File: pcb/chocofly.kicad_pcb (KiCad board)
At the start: 2 copper layers, 317 x 133.4 mm, 142 parts, among them P1 battery+, P2 battery-, SW1 SW_Push, SW11 SW_Push, SW12 SW_Push, SW13 SW_Push, SW14 SW_Push, SW15 SW_Push, SW16 SW_Push, SW17 SW_Push, SW18 SW_Push, SW19 SW_Push, SW2 SW_Push, SW20 SW_Push, SW21 SW_Push, SW22 SW_Push, SW23 SW_Push, SW24 SW_Push, SW25 SW_Push, SW26 SW_Push, SW27 SW_Push, SW28 SW_Push, SW29 SW_Push, SW3 SW_Push, SW30 SW_Push, SW31 SW_Push, SW32 SW_Push, SW33 SW_Push, SW34 SW_Push, SW35 SW_Push, SW36 SW_Push, SW37 SW_Push, SW38 SW_Push, SW39 SW_Push, SW4 SW_Push, SW40 SW_Push, SW41 SW_Push, SW42 SW_Push, SW43 SW_Push, SW44 SW_Push, SW45 SW_Push, SW46 SW_Push, SW47 SW_Push, SW48 SW_Push, SW49 SW_Push, SW5 SW_Push, SW50 SW_Push, SW51 SW_Push, SW52 SW_Push, SW53 SW_Push, SW54 SW_Push, SW55 SW_Push, SW56 SW_Push, SW57 SW_Push, SW58 SW_Push, SW59 SW_Push, SW6 SW_Push, SW60 SW_Push, SW61 SW_Push, SW62 Reset, SW63 Power, SW7 SW_Push, SW8 SW_Push, SW9 SW_Push

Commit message: Edge cuts are so cool.
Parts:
- moved SW63 16.4 mm to (23.8, -18.8)
- moved SW62 16.3 mm to (-22.2, -18.3)
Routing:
- net row0: track 121.0 -> 92.9 mm, vias 5 -> 3
- net row1: track 136.8 -> 109.1 mm, vias 6 -> 4
- net Net-(MCU1-Pad24): track 41.1 -> 24.0 mm
- net Net-(P1-Pad1): track 22.6 -> 6.10 mm, vias 1 -> 0
- net GND: track 83.8 -> 70.5 mm
- net Net-(MCU1-Pad22): track 26.4 -> 14.9 mm
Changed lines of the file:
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@@
   (general
     (thickness 1.6)
-    (drawings 78)
-    (tracks 204)
+    (drawings 79)
+    (tracks 174)
     (zones 0)
     (modules 142)
@@
     (0 F.Cu signal)
     (31 B.Cu signal)
-    (32 B.Adhes user hide)
-    (33 F.Adhes user hide)
-    (34 B.Paste user hide)
-    (35 F.Paste user hide)
-    (36 B.SilkS user hide)
-    (37 F.SilkS user hide)
-    (38 B.Mask user hide)
-    (39 F.Mask user hide)
+    (32 B.Adhes user)
+    (33 F.Adhes user)
+    (34 B.Paste user)
+    (35 F.Paste user)
+    (36 B.SilkS user)
+    (37 F.SilkS user)
+    (38 B.Mask user)
+    (39 F.Mask user)
     (40 Dwgs.User user)
     (41 Cmts.User user)
@@
   )
   (module footprints:Switch_Reset_THT (layer F.Cu)
-    (at -17.979997 -34.039998 346.5)
+    (at -22.229997 -18.289998 346.5)
     (fp_text reference SW62 (at 0.000001 0.01 166.5) (layer Dwgs.User) hide
       (effects (font (size 1 1) (thickness 0.15)))
@@
   )
   (module footprints:Switch_MSK-12C01-07 (layer F.Cu)
-    (at 21.87 -35.11 193.5)
+    (at 23.82 -18.81 193.5)
     (fp_text reference SW63 (at -4.937662 -2.502587 193.5) (layer F.SilkS)
       (effects (font (size 1 1) (thickness 0.15)))
@@
     (pad 1 np_thru_hole circle (at 0 0) (size 2.2 2.2) (drill 2.2) (layers *.Cu *.Mask))
   )
+  (dimension 116.65 (width 0.15) (layer Dwgs.User)
+    (gr_text "116,650 mm" (at 173.7 17.775 90) (layer Dwgs.User)
+      (effects (font (size 1 1) (thickness 0.15)))
+    )
+    (feature1 (pts (xy 152.9 -40.55) (xy 172.986421 -40.55)))
+    (feature2 (pts (xy 152.9 76.1) (xy 172.986421 76.1)))
+    (crossbar (pts (xy 172.4 76.1) (xy 172.4 -40.55)))
+    (arrow1a (pts (xy 172.4 -40.55) (xy 172.986421 -39.423496)))
+    (arrow1b (pts (xy 172.4 -40.55) (xy 171.813579 -39.423496)))
+    (arrow2a (pts (xy 172.4 76.1) (xy 172.986421 74.973496)))
+    (arrow2b (pts (xy 172.4 76.1) (xy 171.813579 74.973496)))
+  )
   (gr_line (start 158.500001 -52.299987) (end 158.500001 -38.85) (layer Edge.Cuts) (width 0.05))
   (gr_arc (start 153.5 -35.53) (end 153.500013 -41.530001) (angle 56.41572066) (layer Edge.Cuts) (width 0.05))
@@
   (gr_line (start -158.5 -35.529996) (end -158.5 5.674075) (layer Edge.Cuts) (width 0.05))
   (gr_text "Chocofly v2.0 by vitvlkv\nhttps://github.com/vlkv/chocofly" (at -96.5 28.9 -13.5) (layer B.SilkS)
-    (effects (font (size 2 2) (thickness 0.3)) (justify left mirror))
+    (effects (font (size 1.8 1.8) (thickness 0.3)) (justify left mirror))
   )
   (gr_text "Chocofly v2.0 by vitvlkv\nhttps://github.com/vlkv/chocofly" (at 98.8 28.5 13.5) (layer F.SilkS)
-    (effects (font (size 2 2) (thickness 0.3)) (justify left))
+    (effects (font (size 1.8 1.8) (thickness 0.3)) (justify left))
   )
-  (gr_text "Power\n" (at 29.05 -37 13.5) (layer F.SilkS)
+  (gr_text "Power\n" (at 31 -20.7 13.5) (layer F.SilkS)
     (effects (font (size 1 1) (thickness 0.15)))
   )
-  (gr_text "Reset\n" (at -24.58 -36.74 -13.5) (layer F.SilkS)
+  (gr_text "Reset\n" (at -28.83 -20.99 -13.5) (layer F.SilkS)
     (effects (font (size 1 1) (thickness 0.15)))
   )
@@
   (via (at 10.200002 -3.821907) (size 0.5) (drill 0.3) (layers F.Cu B.Cu) (net 1))
   (segment (start 7.608095 -3.821905) (end 10.200002 -3.821907) (width 0.25) (layer F.Cu) (net 1) (status 10))
-  (segment (start -17.6 -27.2) (end -17.680619 -27.28062) (width 0.25) (layer B.Cu) (net 1))
-  (segment (start -11.600002 -21.200001) (end -17.6 -27.2) (width 0.25) (layer B.Cu) (net 1))
   (segment (start -11.6 11.4) (end -11.600002 -21.200001) (width 0.25) (layer B.Cu) (net 1))
   (segment (start -8 15.8) (end 10.199999 15.8) (width 0.25) (layer F.Cu) (net 1))
   (segment (start -11.6 12.2) (end -8 15.8) (width 0.25) (layer F.Cu) (net 1))
   (segment (start -11.6 11.4) (end -11.6 12.2) (width 0.25) (layer F.Cu) (net 1))
-  (segment (start -19.8 -29.4) (end -17.6 -27.2) (width 0.25) (layer B.Cu) (net 1))
-  (via (at -18.357145 -29.4) (size 0.5) (drill 0.3) (layers F.Cu B.Cu) (net 1))
-  (via (at 21.797616 -29.397616) (size 0.5) (drill 0.3) (layers F.Cu B.Cu) (net 1))
-  (segment (start 10.199999 -17.799999) (end 21.797616 -29.397616) (width 0.25) (layer B.Cu) (net 1))
   (segment (start 10.199999 -3.8) (end 10.199999 -17.799999) (width 0.25) (layer B.Cu) (net 1))
   (via (at -5.2 -3.8) (size 0.5) (drill 0.3) (layers F.Cu B.Cu) (net 3))
@@
   (segment (start 11 16.599999) (end 11 -1.281905) (width 0.25) (layer B.Cu) (net 16))
   (segment (start 7.608095 -1.281905) (end 11.000004 -1.280008) (width 0.25) (layer F.Cu) (net 16) (status 10))
-  (segment (start 11.000004 -17.338756) (end 15.130624 -21.469375) (width 0.25) (layer B.Cu) (net 16))
-  (segment (start 14.720017 -21.058766) (end 15.130624 -21.469375) (width 0.25) (layer B.Cu) (net 16))
   (segment (start 11.000002 -15.799997) (end 11.000004 -17.338756) (width 0.25) (layer B.Cu) (net 16))
   (segment (start 11.000004 -1.280008) (end 11.000002 -15.799997) (width 0.25) (layer B.Cu) (net 16))
-  (segment (start -18.600002 -26.999998) (end -18.769373 -27.16937) (width 0.25) (layer B.Cu) (net 16))
-  (segment (start -12.400001 -20.799999) (end -18.600002 -26.999998) (width 0.25) (layer B.Cu) (net 16))
   (segment (start -12.4 11.4) (end -12.400001 -20.799999) (width 0.25) (layer B.Cu) (net 16))
   (segment (start 11 16.599999) (end -8.2 16.599999) (width 0.25) (layer F.Cu) (net 16))
@@
   (segment (start -12.4 12.4) (end -8.2 16.599999) (width 0.25) (layer F.Cu) (net 16))
   (segment (start -12.4 11.4) (end -12.4 12.4) (width 0.25) (layer F.Cu) (net 16))
-  (segment (start -20.2 -28.599999) (end -18.600002 -26.999998) (width 0.25) (layer B.Cu) (net 16))
-  (via (at -18.757145 -28.599999) (size 0.5) (drill 0.3) (layers F.Cu B.Cu) (net 16))
-  (segment (start 15.130624 -21.469375) (end 22.2 -28.6) (width 0.25) (layer B.Cu) (net 16))
-  (via (at 22.2 -28.6) (size 0.5) (drill 0.3) (layers F.Cu B.Cu) (net 16))
   (via (at -13.2 11.399999) (size 0.5) (drill 0.3) (layers F.Cu B.Cu) (net 29))
   (via (at 11.799999 17.397562) (size 0.5) (drill 0.3) (layers F.Cu B.Cu) (net 29))
@@
   (segment (start -7.631905 -13.981905) (end 0.581905 -13.981905) (width 0.5) (layer F.Cu) (net 80) (status 10))
   (segment (start 4.181905 -13.981905) (end 6.6 -16.4) (width 0.5) (layer F.Cu) (net 80))
-  (segment (start 18.4 -22.8) (end 12 -16.4) (width 0.5) (layer F.Cu) (net 80))
   (segment (start 6.6 -16.4) (end 12 -16.4) (width 0.5) (layer F.Cu) (net 80))
-  (segment (start 18.4 -30.8) (end 18.4 -22.8) (width 0.5) (layer F.Cu) (net 80))
   (segment (start -7.574381 -8.844388) (end -7.619991 -8.890005) (width 0.5) (layer F.Cu) (net 81) (status 30))
   (segment (start -10 -11.27) (end -7.631904 -8.901906) (width 0.25) (layer B.Cu) (net 81) (status 20))
@@
   (segment (start -10 -12.2) (end -10 -11.27) (width 0.25) (layer B.Cu) (net 81))
   (segment (start -10 -22) (end -10 -12.2) (width 0.25) (layer B.Cu) (net 81))
-  (segment (start -17.97999 -29.979992) (end -12.4 -24.400001) (width 0.25) (layer B.Cu) (net 81))
-  (segment (start -12.4 -24.400001) (end -10 -22) (width 0.25) (layer B.Cu) (net 81))
-  (segment (start -12.530625 -24.530629) (end -12.4 -24.400001) (width 0.25) (layer B.Cu) (net 81))
   (segment (start 7.608091 -6.361908) (end 7.608095 -8.901905) (width 0.5) (layer B.Cu) (net 82) (status 30))
   (via (at -10.799999 -11.440022) (size 0.5) (drill 0.3) (layers F.Cu B.Cu) (net 82))
@@
   (segment (start -7.631905 -11.441905) (end -10.799999 -11.440022) (width 0.25) (layer F.Cu) (net 82) (status 10))
   (segment (start -10.8 -21.6) (end -10.799995 14.4) (width 0.25) (layer B.Cu) (net 82))
-  (segment (start -16.000002 -26.799999) (end -10.8 -21.6) (width 0.25) (layer B.Cu) (net 82))
-  (segment (start -18.779986 -29.579984) (end -16.000002 -26.799999) (width 0.25) (layer B.Cu) (net 82))
-  (segment (start -16.369376 -27.169373) (end -16.000002 -26.799999) (width 0.25) (layer B.Cu) (net 82))
-  (segment (start -21.140199 -34.798696) (end -20.538696 -34.798697) (width 0.25) (layer B.Cu) (net 82) (status 30))
-  (segment (start -21.140199 -34.798696) (end -20.738696 -34.798696) (width 0.25) (layer B.Cu) (net 82) (status 30))
-  (segment (start -21.140199 -34.798696) (end -20.718682 -34.798696) (width 0.25) (layer B.Cu) (net 82) (status 30))
   (segment (start 0.540001 -8.901905) (end -2 -11.441906) (width 0.5) (layer F.Cu) (net 82))
   (segment (start 7.608095 -8.901905) (end 0.540001 -8.901905) (width 0.5) (layer F.Cu) (net 82) (status 10))
@@
   (segment (start 4 -16.6) (end 7.30125 -16.6) (width 0.5) (layer B.Cu) (net 83) (status 10))
   (segment (start 7.620014 -16.918764) (end 8.450625 -17.749375) (width 0.5) (layer B.Cu) (net 83))
-  (segment (start 16.634229 -30.834229) (end 16.634229 -26.034229) (width 0.5) (layer F.Cu) (net 83))
-  (via (at 16.634229 -26.034229) (size 0.6) (drill 0.4) (layers F.Cu B.Cu) (net 83))
-  (segment (start 16.634229 -25.965771) (end 16.650625 -25.949375) (width 0.5) (layer B.Cu) (net 83))
-  (segment (start 16.634229 -26.034229) (end 16.634229 -25.965771) (width 0.5) (layer B.Cu) (net 83))
-  (segment (start 8.450625 -17.749375) (end 16.650625 -25.949375) (width 0.5) (layer B.Cu) (net 83))
 )

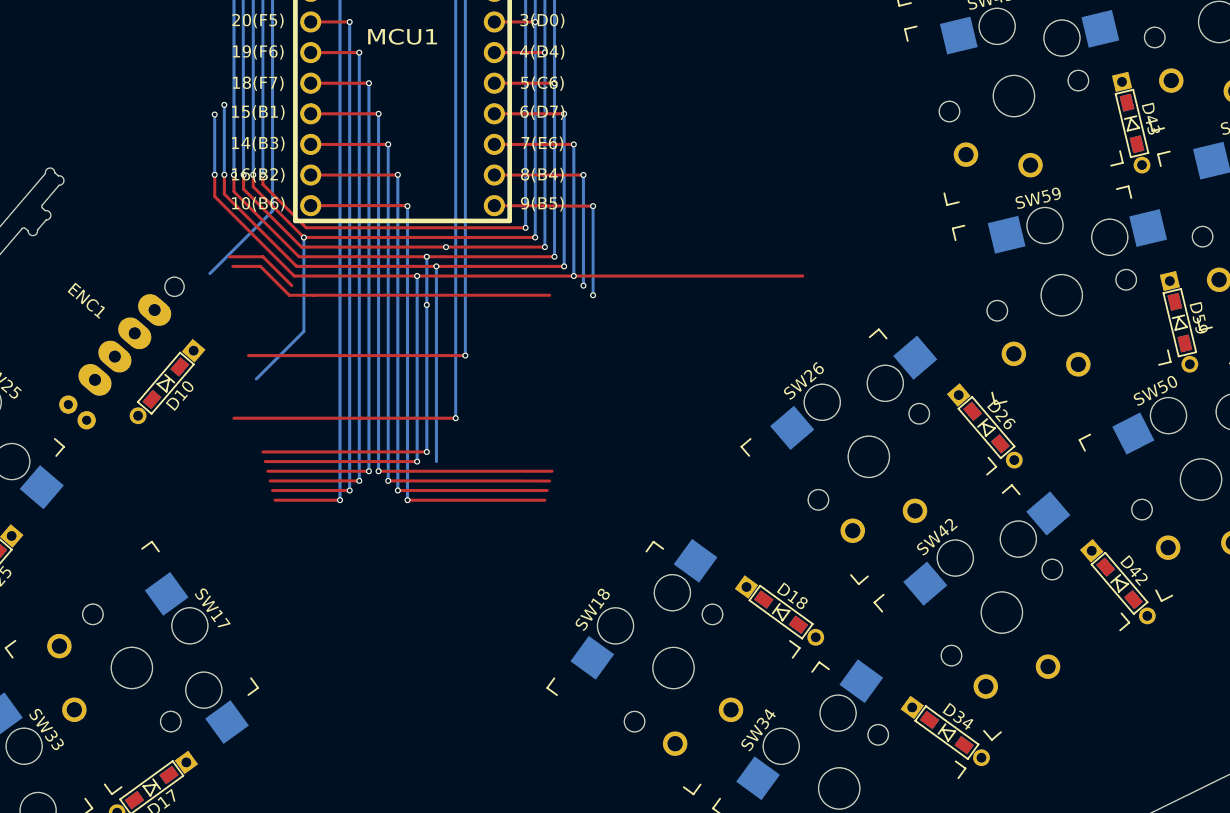
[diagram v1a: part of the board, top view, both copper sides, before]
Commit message: Added one more encoder
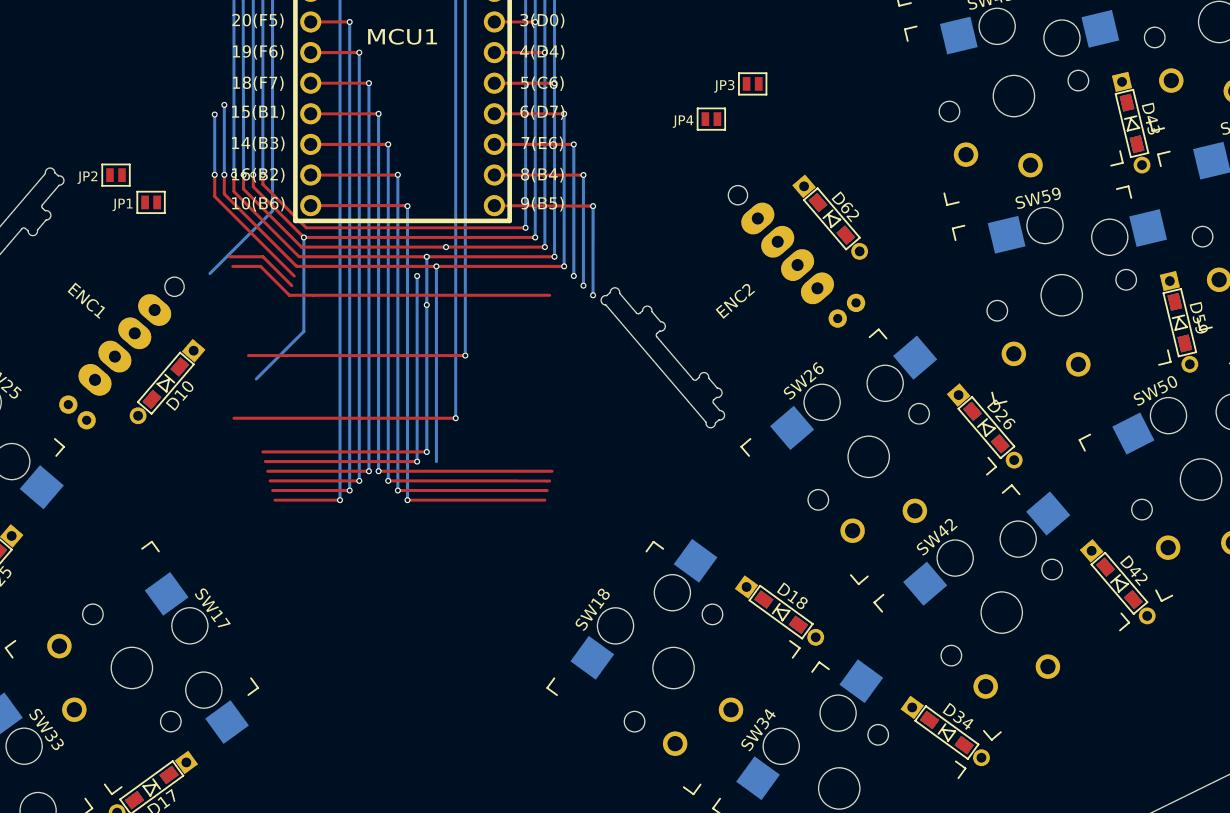
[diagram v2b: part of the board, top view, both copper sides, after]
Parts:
- added D62: 1N4148, footprints:diode_TH_SMD, F.Cu at (35.6, 15.1)
- added ENC2: EVQWGD001, footprints:EVQWGD001, F.Cu at (27.6, 21.9)
- added JP1: Jumper_NC_Small, footprints:avalanche_Jumper, F.Cu at (-20.9, 13.7)
- added JP2: Jumper_NC_Small, footprints:avalanche_Jumper, F.Cu at (-23.8, 11.4)
- added JP3: Jumper_NC_Small, footprints:avalanche_Jumper, F.Cu at (29.0, 3.86)
- added JP4: Jumper_NC_Small, footprints:avalanche_Jumper, F.Cu at (25.6, 6.78)
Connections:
- ENC1 pad A: encA -> Net-(ENC1-PadA)
- ENC1 pad B: encB -> Net-(ENC1-PadB)
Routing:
- net row5: track 103.8 -> 61.6 mm

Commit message: Ready to wire
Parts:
- moved H15 252.4 mm to (-70.1, 150.4), turned to 0 degrees
- moved H11 240.7 mm to (-76.1, 150.4), turned to 0 degrees
- moved H22 216.8 mm to (-58.2, 150.4)
- moved H4 209.9 mm to (-82.0, 150.4)
- moved H2 185.6 mm to (-82.0, 144.4)
- moved H10 152.2 mm to (-70.1, 138.5)
- moved H18 151.4 mm to (-58.2, 138.5)
- moved H1 125.5 mm to (-82.0, 138.5)
- moved H13 97.7 mm to (-64.2, 138.5)
- moved H16 91.3 mm to (-64.2, 144.4), turned to 0 degrees
- moved H3 90.2 mm to (-76.1, 138.5), turned to 0 degrees
- moved H21 87.6 mm to (-58.2, 144.4)
- moved H6 74.7 mm to (-76.1, 144.4)
- moved H12 63.0 mm to (-70.1, 144.4)
- moved H20 22.6 mm to (-64.2, 150.4)
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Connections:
- JP1 pad 1: encA -> Net-(ENC1-PadA)
- JP1 pad 2: Net-(ENC1-PadA) -> encA
- JP2 pad 1: encB -> Net-(ENC1-PadB)
- JP2 pad 2: Net-(ENC1-PadB) -> encB
- JP3 pad 1: encA -> Net-(ENC2-PadA)
- JP3 pad 2: Net-(ENC2-PadA) -> encA
- JP4 pad 1: encB -> Net-(ENC2-PadB)
- JP4 pad 2: Net-(ENC2-PadB) -> encB
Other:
- outline, holes or cut-outs redrawn
- board text added: "Angle 4 degrees Angle 13,5 degrees"

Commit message: Wiring...
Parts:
- moved H18 60.8 mm to (-87.7, 85.3), turned to 13.5 degrees
- moved H21 60.3 mm to (-86.3, 91.1), turned to 13.5 degrees
- moved H22 59.8 mm to (-85.0, 96.9), turned to 13.5 degrees
- moved H13 59.5 mm to (-93.5, 86.7), turned to 13.5 degrees
- moved H16 59.0 mm to (-92.1, 92.5), turned to 13.5 degrees
- moved H20 58.5 mm to (-90.7, 98.3), turned to 13.5 degrees
- moved H10 58.2 mm to (-99.3, 88.1), turned to 13.5 degrees
- moved H12 57.7 mm to (-97.9, 93.9), turned to 13.5 degrees
- moved H15 57.2 mm to (-96.5, 99.7), turned to 13.5 degrees
- moved H3 56.9 mm to (-105.1, 89.5), turned to 13.5 degrees
- moved H6 56.4 mm to (-103.7, 95.3), turned to 13.5 degrees
- moved H11 55.9 mm to (-102.3, 101.1), turned to 13.5 degrees
- moved H1 55.7 mm to (-110.9, 90.9), turned to 13.5 degrees
- moved H2 55.1 mm to (-109.5, 96.7), turned to 13.5 degrees
- moved H4 54.6 mm to (-108.1, 102.4), turned to 13.5 degrees
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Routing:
- net col2: track 46.9 -> 297.4 mm
- net col0: track 50.1 -> 293.8 mm
- net col1: track 48.7 -> 289.5 mm
- net row0: track 92.9 -> 222.4 mm
- net row2: track 85.2 -> 205.4 mm
- net row6: track 22.8 -> 142.2 mm
- net row4: track 72.7 -> 191.9 mm
- net row1: track 109.1 -> 216.6 mm
- net row5: track 61.6 -> 156.7 mm
- net row3: track 117.0 -> 210.2 mm
- net row7: track 42.7 -> 135.9 mm
- net Net-(D46-Pad2): track 0.00 -> 26.6 mm
- net Net-(D7-Pad2): track 0.00 -> 26.6 mm
- net Net-(D1-Pad2): track 0.00 -> 26.6 mm
- net Net-(D16-Pad2): track 0.00 -> 26.6 mm
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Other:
- board size 317 x 133.4 mm -> 322.4 x 174.6 mm

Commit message: WIP
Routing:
- net col3: track 45.4 -> 81.8 mm
- net row7: track 135.9 -> 165.5 mm
- net Net-(D57-Pad2): track 0.00 -> 26.6 mm
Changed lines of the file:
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@@
     (thickness 1.6)
     (drawings 83)
-    (tracks 775)
+    (tracks 802)
     (zones 0)
     (modules 148)
@@
     (38 B.Mask user)
     (39 F.Mask user)
-    (40 Dwgs.User user hide)
-    (41 Cmts.User user hide)
-    (42 Eco1.User user hide)
+    (40 Dwgs.User user)
+    (41 Cmts.User user)
+    (42 Eco1.User user)
     (43 Eco2.User user)
     (44 Edge.Cuts user)
@@
   (segment (start -51.461364 27.622196) (end -51.461364 36.197196) (width 0.25) (layer B.Cu) (net 62))
   (segment (start -39.436364 41.622195) (end -39.436364 39.847195) (width 0.25) (layer B.Cu) (net 62))
+  (segment (start -78.851364 51.427195) (end -75.576364 54.702195) (width 0.25) (layer B.Cu) (net 63))
+  (segment (start -78.851364 42.852195) (end -78.851364 51.427195) (width 0.25) (layer B.Cu) (net 63))
+  (segment (start -66.576363 56.852196) (end -66.576363 55.077196) (width 0.25) (layer F.Cu) (net 63))
+  (segment (start -73.426363 56.852196) (end -75.576364 54.702195) (width 0.25) (layer F.Cu) (net 63))
+  (segment (start -66.576363 56.852196) (end -73.426363 56.852196) (width 0.25) (layer F.Cu) (net 63))
+  (segment (start -66.576363 56.852196) (end -66.576363 55.077196) (width 0.25) (layer B.Cu) (net 63))
   (via (at -4.577683 -0.219325) (size 0.5) (drill 0.3) (layers F.Cu B.Cu) (net 67))
   (segment (start -4.577683 -0.219325) (end 4.499118 37.588269) (width 0.25) (layer B.Cu) (net 67))
@@
   (segment (start -6.534388 5.474786) (end -1.834136 4.346354) (width 0.25) (layer F.Cu) (net 69) (status 10))
   (segment (start -2.486509 37.619904) (end 5.681397 35.658964) (width 0.25) (layer F.Cu) (net 69))
+  (segment (start -65.751364 45.052195) (end -64.2 46.603559) (width 0.25) (layer B.Cu) (net 69))
+  (segment (start -67.301364 45.052195) (end -65.751364 45.052195) (width 0.25) (layer B.Cu) (net 69))
+  (segment (start -64.2 51.058892) (end -61.592315 53.666577) (width 0.25) (layer B.Cu) (net 69))
+  (segment (start -64.2 46.603559) (end -64.2 51.058892) (width 0.25) (layer B.Cu) (net 69))
+  (segment (start -80.576364 52.602195) (end -74.578559 58.6) (width 0.25) (layer F.Cu) (net 69))
+  (segment (start -61.592315 53.666577) (end -61.592315 55.192315) (width 0.25) (layer F.Cu) (net 69))
+  (segment (start -65 58.6) (end -65.2 58.6) (width 0.25) (layer F.Cu) (net 69))
+  (segment (start -61.592315 55.192315) (end -65 58.6) (width 0.25) (layer F.Cu) (net 69))
+  (segment (start -65.2 58.6) (end -65.1 58.6) (width 0.25) (layer F.Cu) (net 69))
+  (segment (start -74.578559 58.6) (end -65.2 58.6) (width 0.25) (layer F.Cu) (net 69))
   (via (at -0.46514 6.629865) (size 0.5) (drill 0.3) (layers F.Cu B.Cu) (net 70))
   (via (at 6.459294 35.472208) (size 0.5) (drill 0.3) (layers F.Cu B.Cu) (net 70))
@@
   (segment (start -39.436364 34.522195) (end -36.122195 34.522195) (width 0.25) (layer F.Cu) (net 77))
   (segment (start -39.436364 36.297195) (end -39.436364 34.522195) (width 0.25) (layer B.Cu) (net 77))
+  (segment (start -66.576363 51.527196) (end -66.576363 49.752196) (width 0.25) (layer F.Cu) (net 77))
+  (segment (start -66.576363 51.527196) (end -66.576363 49.752196) (width 0.25) (layer B.Cu) (net 77))
+  (segment (start -73.8 35.7) (end -73.8 32.45856) (width 0.25) (layer B.Cu) (net 77))
+  (segment (start -73 46.1) (end -73 36.5) (width 0.25) (layer B.Cu) (net 77))
+  (segment (start -74.461364 31.797196) (end -75.186364 31.797196) (width 0.25) (layer B.Cu) (net 77))
+  (segment (start -73 36.5) (end -73.8 35.7) (width 0.25) (layer B.Cu) (net 77))
+  (segment (start -72.6 46.5) (end -73 46.1) (width 0.25) (layer B.Cu) (net 77))
+  (segment (start -73.8 32.45856) (end -74.461364 31.797196) (width 0.25) (layer B.Cu) (net 77))
+  (segment (start -72.6 49.5) (end -72.6 46.5) (width 0.25) (layer B.Cu) (net 77))
+  (segment (start -70.572804 51.527196) (end -72.6 49.5) (width 0.25) (layer B.Cu) (net 77))
+  (segment (start -66.576363 51.527196) (end -70.572804 51.527196) (width 0.25) (layer B.Cu) (net 77))
   (segment (start 4.070815 31.520604) (end -6.236305 33.995124) (width 0.25) (layer F.Cu) (net 78))
   (via (at 11.655301 29.69973) (size 0.5) (drill 0.3) (layers F.Cu B.Cu) (net 78))

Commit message: WIP
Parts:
- moved D53 106.0 mm to (95.9, -119.5), turned to 333.5 degrees
- moved D6 104.4 mm to (50.2, -142.2), turned to 333.5 degrees
- moved D37 104.2 mm to (80.7, -127.1), turned to 333.5 degrees
- moved D21 103.6 mm to (65.4, -134.7), turned to 333.5 degrees
- moved H4 103.1 mm to (-15.7, 148.1), turned to 54 degrees
- moved H2 101.1 mm to (-20.5, 144.6), turned to 54 degrees
- moved H11 99.5 mm to (-12.2, 143.3), turned to 54 degrees
- moved SW46 99.3 mm to (-80.8, 118.6), turned to 44.5 degrees
- moved SW53 99.3 mm to (87.8, -113.4), turned to 63.5 degrees
- moved H1 99.2 mm to (-25.3, 141.1), turned to 54 degrees
- moved SW1 98.7 mm to (-116.5, 82.2), turned to 44.5 degrees
- moved SW6 98.7 mm to (42.2, -136.2), turned to 63.5 degrees
- moved SW30 97.7 mm to (-92.7, 106.5), turned to 44.5 degrees
- moved SW37 97.7 mm to (72.6, -121.0), turned to 63.5 degrees
- moved SW14 97.5 mm to (-104.6, 94.3), turned to 44.5 degrees
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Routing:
- net col3: track 81.8 -> 207.8 mm
- net row5: track 156.7 -> 191.9 mm
- net row6: track 142.2 -> 173.0 mm
- net Net-(D41-Pad2): track 0.00 -> 26.6 mm
- net Net-(D25-Pad2): track 0.00 -> 26.6 mm
- net Net-(D49-Pad2): track 0.00 -> 26.6 mm
- net row3: track 210.2 -> 228.7 mm
- net Net-(ENC1-PadA): track 0.00 -> 12.4 mm
- net Net-(ENC1-PadB): track 0.00 -> 11.9 mm
- net GND: track 70.5 -> 80.8 mm
- net row1: track 216.6 -> 226.4 mm
- net Net-(D10-Pad2): track 0.00 -> 8.48 mm
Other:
- board size 322.4 x 174.6 mm -> 242.8 x 295 mm
